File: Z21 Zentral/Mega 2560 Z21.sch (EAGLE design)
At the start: 144 parts, among them IC1 TLE5205-2G, IC2 74AC244DW, IC3 LM358D, IC5 FT232RL, IC6 LTC485S, J1 RJ11, J2 RJ11, J3 RJ11, J5 RJ45-6L-B, J6 USB_MINI-B_SMT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

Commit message: Add files via upload
Changed 6 way power connector to allow connector to fit
Added PFET on input instead of Diode
Tidied up PCB Legends
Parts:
- removed D1: P600, diode:P600
- added D5: (no value), diode:ZENER-DIODESOT23
- added Q9: FDD4141TO252, transistor-fet:FDD4141TO252
- added R31: 100k, rcl:R-EU_R0603
- X9: device con-wago-508:W237-06P -> con-wago-500:W237-136
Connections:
- new net N$22: D5.A, Q9.G, R31.1
- net +18V: now also D5.C, Q9.S; no longer D1.C
- net GND: now also R31.2
- net N$23: now also Q9.D; no longer D1.A
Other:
- moved on the sheet: B1, C10, C11, C27, C3, C4, C5, C6, C9, F1, IC3B, U$2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

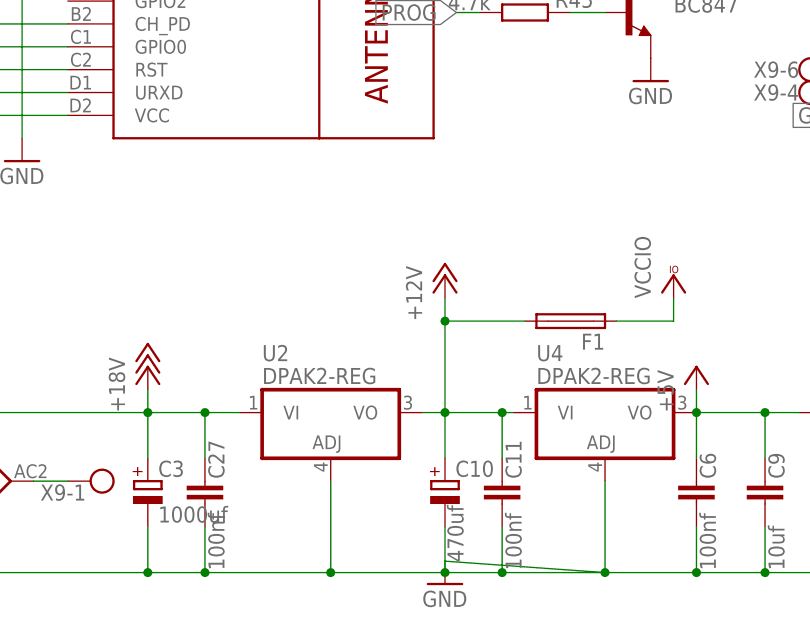
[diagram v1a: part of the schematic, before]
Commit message: Add files via upload
Added P Channel FET, replacing Diode
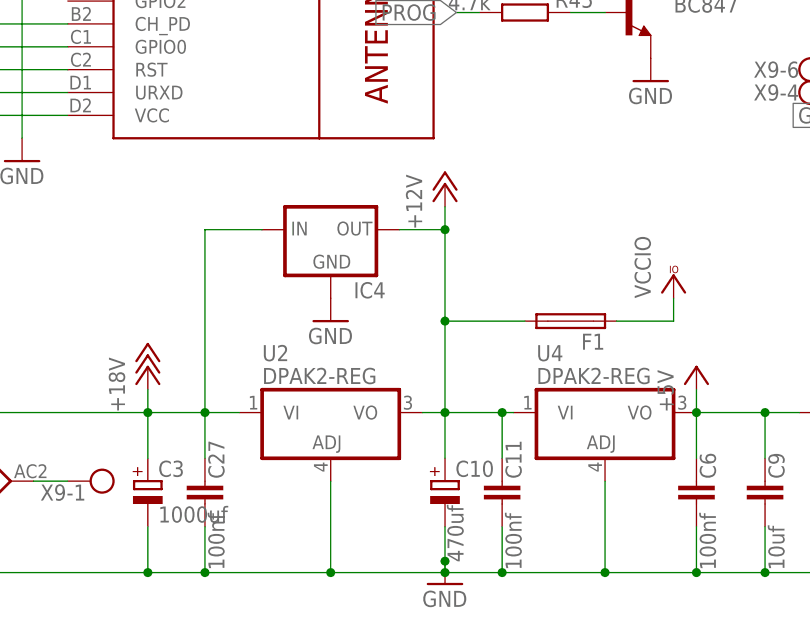
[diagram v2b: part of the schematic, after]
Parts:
- added IC4: (no value), v-reg:78XXS
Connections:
- net +12V: now also IC4.OUT
- net +18V: now also IC4.IN
- net GND: now also IC4.GND

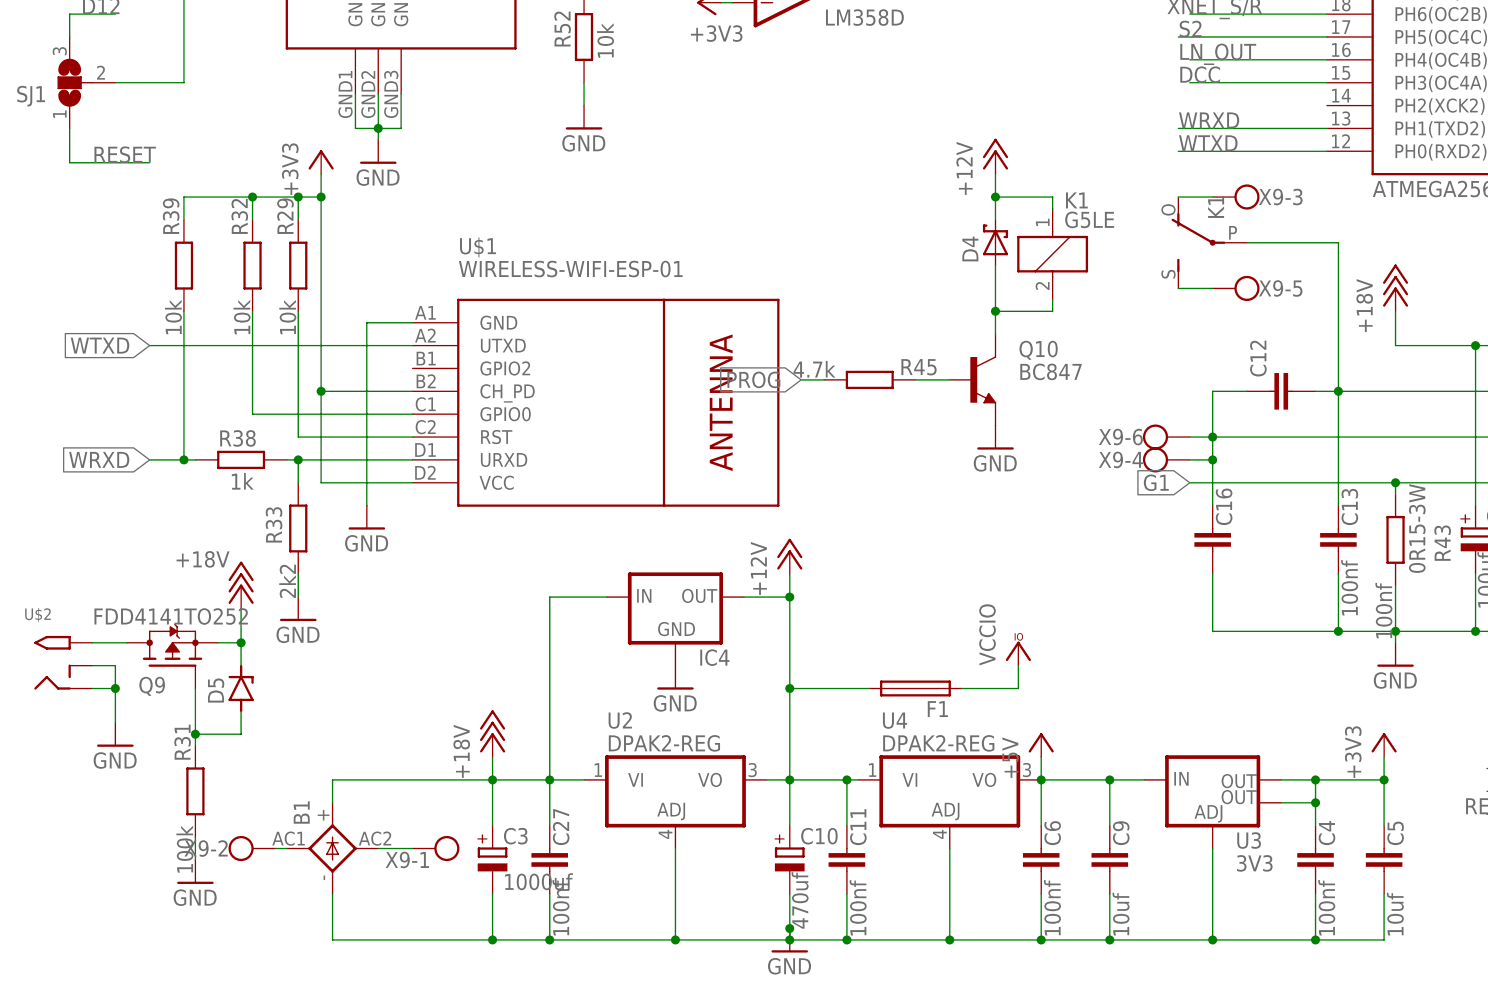
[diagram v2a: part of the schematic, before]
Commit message: Changed power connector and minor moves of components
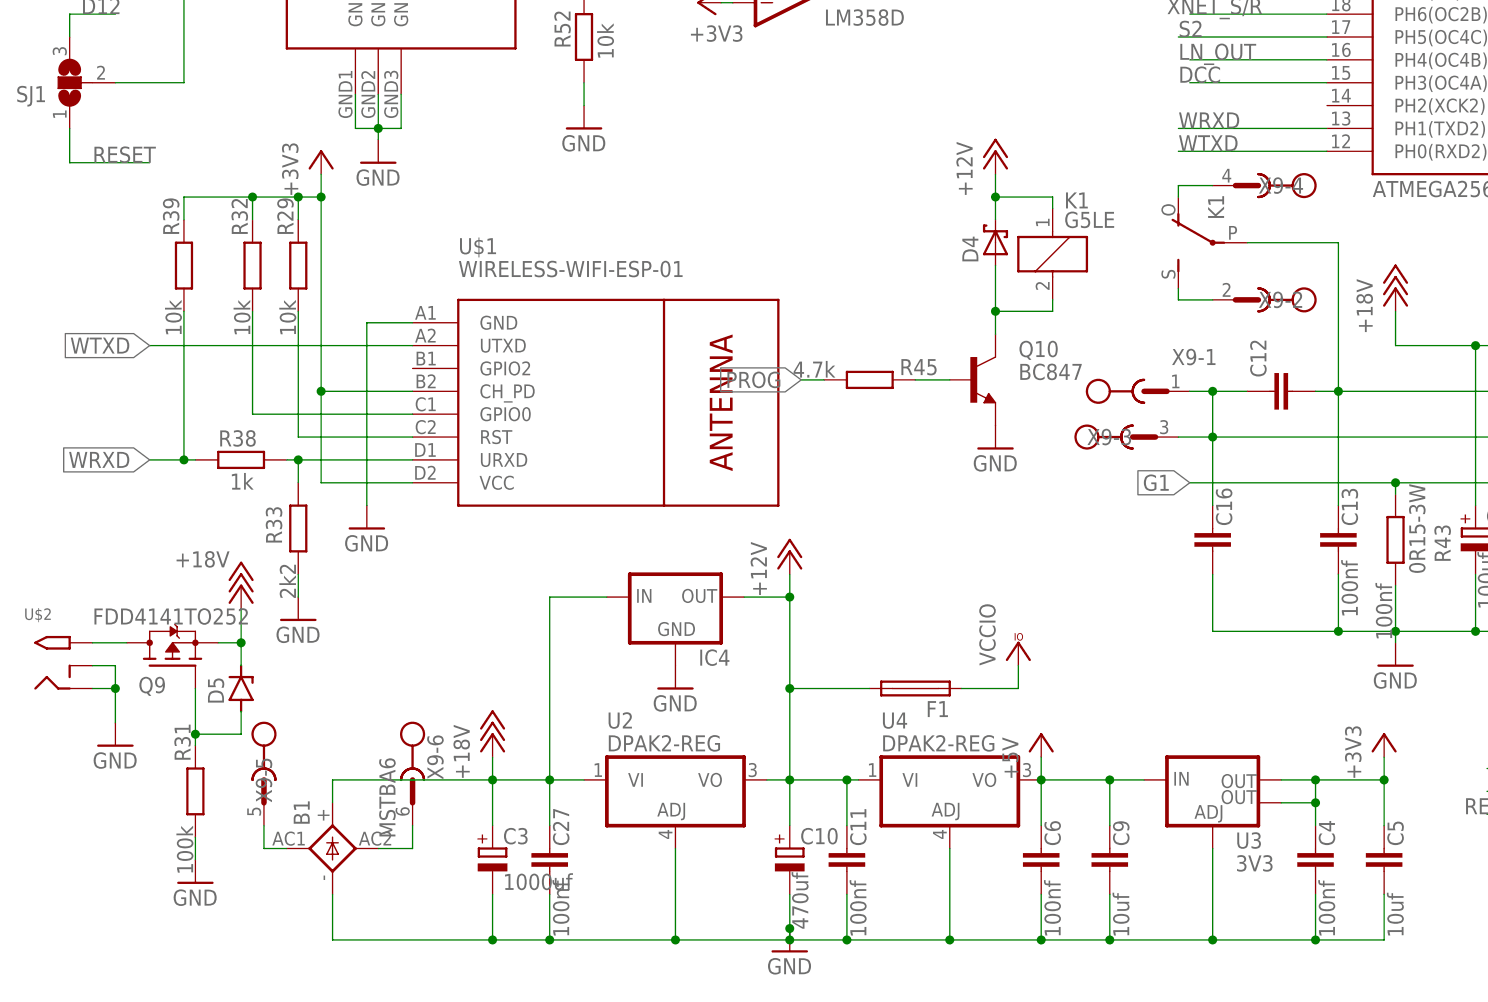
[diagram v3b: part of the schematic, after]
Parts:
- X9: value (none) -> MSTBA6; device con-wago-500:W237-136 -> con-phoenix-508:MSTBA6
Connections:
- net N$26: now also X9-1.1, X9-3.1; no longer X9-4.KL, X9-6.KL
- net N$32: now also K12.S, X9-2.1; no longer B1.AC1, X9-2.KL
- net N$34: now also X9-6.1; no longer X9-1.KL
- net N$37: now also X9-4.1; no longer X9-3.KL
- net N$40: now also B1.AC1, X9-5.1; no longer K12.S, X9-5.KL
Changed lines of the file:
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@@
 <?xml version="1.0" encoding="utf-8"?>
 <!DOCTYPE eagle SYSTEM "eagle.dtd">
-<eagle version="9.4.2">
+<eagle version="9.6.0">
 <drawing>
 <settings>
@@
 <part name="P+18" library="supply1" library_urn="urn:adsk.eagle:library:371" deviceset="+18V" device=""/>
 <part name="R27" library="rcl" deviceset="R-EU_" device="R0603" value="22k"/>
-<part name="X9" library="con-wago-500" library_urn="urn:adsk.eagle:library:195" deviceset="W237-136" device="" package3d_urn="urn:adsk.eagle:package:10693/1"/>
+<part name="X9" library="con-phoenix-508" library_urn="urn:adsk.eagle:library:176" deviceset="MSTBA6" device="" package3d_urn="urn:adsk.eagle:package:9616/1"/>
 <part name="U$1" library="diy-modules" deviceset="WIRELESS-WIFI-ESP-01" device=""/>
 <part name="GND23" library="supply1" library_urn="urn:adsk.eagle:library:371" deviceset="GND" device=""/>
@@
 <attribute name="VALUE" x="16.002" y="162.56" size="1.778" layer="96" rot="R90"/>
 </instance>
-<instance part="X9" gate="-1" x="53.34" y="17.78" smashed="yes" rot="R180">
-<attribute name="NAME" x="50.292" y="17.399" size="1.778" layer="95" rot="R180"/>
+<instance part="X9" gate="-1" x="129.54" y="68.58" smashed="yes">
+<attribute name="NAME" x="132.588" y="71.501" size="1.778" layer="95"/>
 </instance>
-<instance part="X9" gate="-2" x="27.94" y="17.78" smashed="yes">
-<attribute name="NAME" x="27.94" y="18.669" size="1.778" layer="95" rot="R180"/>
+<instance part="X9" gate="-2" x="142.24" y="78.74" smashed="yes" rot="R180">
+<attribute name="NAME" x="142.24" y="77.851" size="1.778" layer="95"/>
 </instance>
-<instance part="X9" gate="-3" x="142.24" y="90.17" smashed="yes" rot="R180">
-<attribute name="NAME" x="142.24" y="89.281" size="1.778" layer="95"/>
+<instance part="X9" gate="-3" x="128.27" y="63.5" smashed="yes">
+<attribute name="NAME" x="128.27" y="64.389" size="1.778" layer="95" rot="R180"/>
 </instance>
-<instance part="X9" gate="-4" x="129.54" y="60.96" smashed="yes">
-<attribute name="NAME" x="129.54" y="61.849" size="1.778" layer="95" rot="R180"/>
+<instance part="X9" gate="-4" x="142.24" y="91.44" smashed="yes" rot="R180">
+<attribute name="NAME" x="142.24" y="90.551" size="1.778" layer="95"/>
 </instance>
 <instance part="U$1" gate="G$1" x="71.12" y="66.04" smashed="yes">
@@
 <attribute name="VALUE" x="110.49" y="59.69" size="1.778" layer="96"/>
 </instance>
-<instance part="X9" gate="-5" x="142.24" y="80.01" smashed="yes" rot="R180">
-<attribute name="NAME" x="142.24" y="79.121" size="1.778" layer="95"/>
+<instance part="X9" gate="-5" x="31.75" y="25.4" smashed="yes" rot="R270">
+<attribute name="NAME" x="32.639" y="22.86" size="1.778" layer="95" rot="R90"/>
 </instance>
-<instance part="X9" gate="-6" x="129.54" y="63.5" smashed="yes">
-<attribute name="VALUE" x="127" y="59.817" size="1.778" layer="96"/>
-<attribute name="NAME" x="129.54" y="64.389" size="1.778" layer="95" rot="R180"/>
+<instance part="X9" gate="-6" x="48.26" y="25.4" smashed="yes" rot="R270">
+<attribute name="VALUE" x="44.577" y="27.94" size="1.778" layer="96" rot="R270"/>
+<attribute name="NAME" x="51.689" y="25.4" size="1.778" layer="95" rot="R90"/>
 </instance>
 <instance part="JP3" gate="G$1" x="335.28" y="73.66" smashed="yes" rot="MR90">
@@
 <wire x1="137.16" y1="68.58" x2="140.97" y2="68.58" width="0.1524" layer="91"/>
 <pinref part="C16" gate="G$1" pin="1"/>
-<wire x1="137.16" y1="55.88" x2="137.16" y2="60.96" width="0.1524" layer="91"/>
+<wire x1="137.16" y1="55.88" x2="137.16" y2="63.5" width="0.1524" layer="91"/>
 <junction x="137.16" y="63.5"/>
-<wire x1="137.16" y1="60.96" x2="137.16" y2="63.5" width="0.1524" layer="91"/>
-<wire x1="134.62" y1="60.96" x2="137.16" y2="60.96" width="0.1524" layer="91"/>
-<junction x="137.16" y="60.96"/>
-<pinref part="X9" gate="-4" pin="KL"/>
-<pinref part="X9" gate="-6" pin="KL"/>
-<wire x1="137.16" y1="63.5" x2="134.62" y2="63.5" width="0.1524" layer="91"/>
+<pinref part="X9" gate="-1" pin="1"/>
+<wire x1="134.62" y1="68.58" x2="137.16" y2="68.58" width="0.1524" layer="91"/>
+<junction x="137.16" y="68.58"/>
+<pinref part="X9" gate="-3" pin="1"/>
+<wire x1="133.35" y1="63.5" x2="137.16" y2="63.5" width="0.1524" layer="91"/>
 </segment>
 </net>
@@
 </segment>
 </net>
-<net name="N$32" class="0">
-<segment>
-<pinref part="X9" gate="-2" pin="KL"/>
-<pinref part="B1" gate="G$1" pin="AC1"/>
-<wire x1="33.02" y1="17.78" x2="34.29" y2="17.78" width="0.1524" layer="91"/>
-</segment>
-</net>
-<net name="N$34" class="0">
-<segment>
-<pinref part="B1" gate="G$1" pin="AC2"/>
-<pinref part="X9" gate="-1" pin="KL"/>
-<wire x1="44.45" y1="17.78" x2="48.26" y2="17.78" width="0.1524" layer="91"/>
-</segment>
-</net>
 <net name="PROG" class="0">
 <segment>
@@
 </segment>
 </net>
-<net name="N$37" class="0">
-<segment>
-<pinref part="X9" gate="-3" pin="KL"/>
-<wire x1="133.35" y1="90.17" x2="137.16" y2="90.17" width="0.1524" layer="91"/>
-<pinref part="K1" gate="2" pin="O"/>
-</segment>
-</net>
-<net name="N$40" class="0">
-<segment>
-<pinref part="X9" gate="-5" pin="KL"/>
-<wire x1="133.35" y1="80.01" x2="137.16" y2="80.01" width="0.1524" layer="91"/>
-<pinref part="K1" gate="2" pin="S"/>
-</segment>
-</net>
 <net name="N$42" class="0">
 <segment>
@@
 </segment>
 </net>
+<net name="N$34" class="0">
+<segment>
+<pinref part="B1" gate="G$1" pin="AC2"/>
+<wire x1="44.45" y1="17.78" x2="48.26" y2="17.78" width="0.1524" layer="91"/>
+<pinref part="X9" gate="-6" pin="1"/>
+<wire x1="48.26" y1="17.78" x2="48.26" y2="20.32" width="0.1524" layer="91"/>
+</segment>
+</net>
+<net name="N$32" class="0">
+<segment>
+<pinref part="X9" gate="-2" pin="1"/>
+<wire x1="137.16" y1="78.74" x2="133.35" y2="78.74" width="0.1524" layer="91"/>
+<pinref part="K1" gate="2" pin="S"/>
+<wire x1="133.35" y1="80.01" x2="133.35" y2="78.74" width="0.1524" layer="91"/>
+</segment>
+</net>
+<net name="N$40" class="0">
+<segment>
+<pinref part="X9" gate="-5" pin="1"/>
+<pinref part="B1" gate="G$1" pin="AC1"/>
+<wire x1="31.75" y1="20.32" x2="31.75" y2="17.78" width="0.1524" layer="91"/>
+<wire x1="31.75" y1="17.78" x2="34.29" y2="17.78" width="0.1524" layer="91"/>
+</segment>
+</net>
+<net name="N$37" class="0">
+<segment>
+<pinref part="K1" gate="2" pin="O"/>
+<pinref part="X9" gate="-4" pin="1"/>
+<wire x1="133.35" y1="90.17" x2="133.35" y2="91.44" width="0.1524" layer="91"/>
+<wire x1="133.35" y1="91.44" x2="137.16" y2="91.44" width="0.1524" layer="91"/>
+</segment>
+</net>
